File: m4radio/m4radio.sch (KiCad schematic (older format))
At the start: 71 parts, among them IC1 NCP4620, IC10 Si4460, IC2 MCP2562, IC3 STM32F405RxTx, IC4 MAX-M8Q, IC5 NC7SZ04, IC6 NCP380, IC7 CS2100-CP, IC8 SL18860DC, IC9 SN74LVC1G0832, J1 WEST TOP, J2 EAST TOP, P1 SWD_TC, P2 COAX, P3 COAX, Y1 TCXO

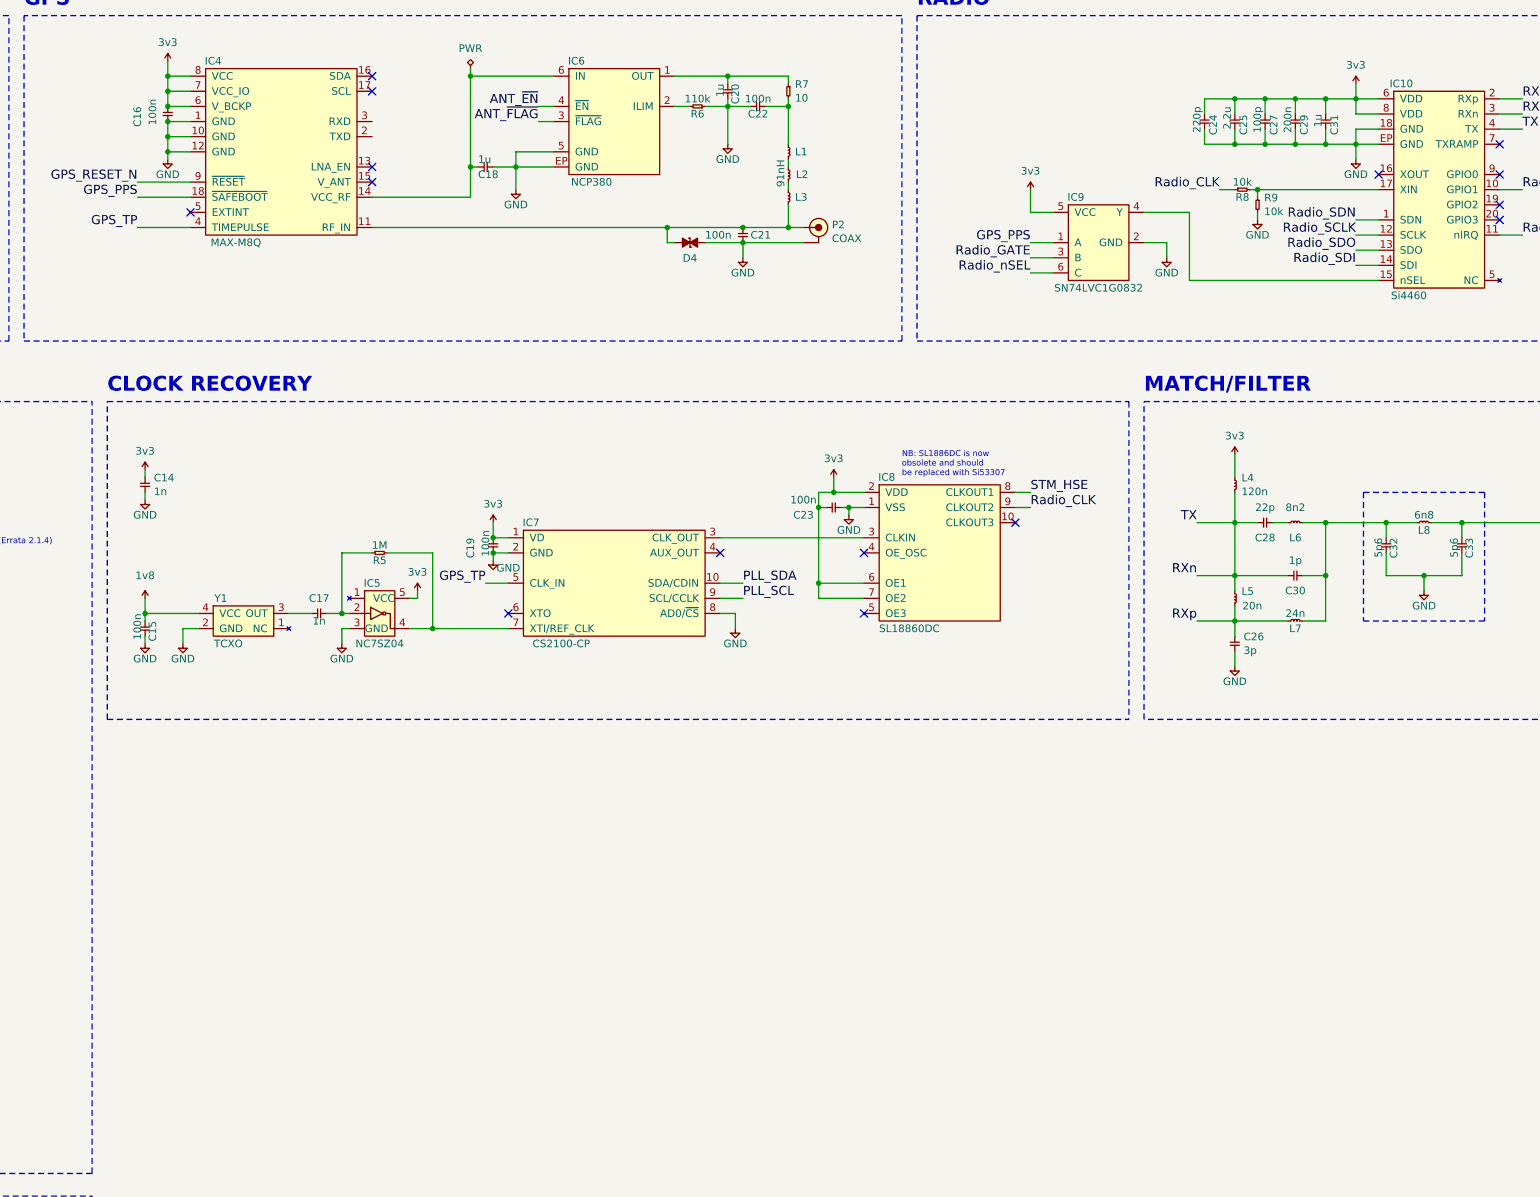
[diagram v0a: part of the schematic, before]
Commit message: Add power amp
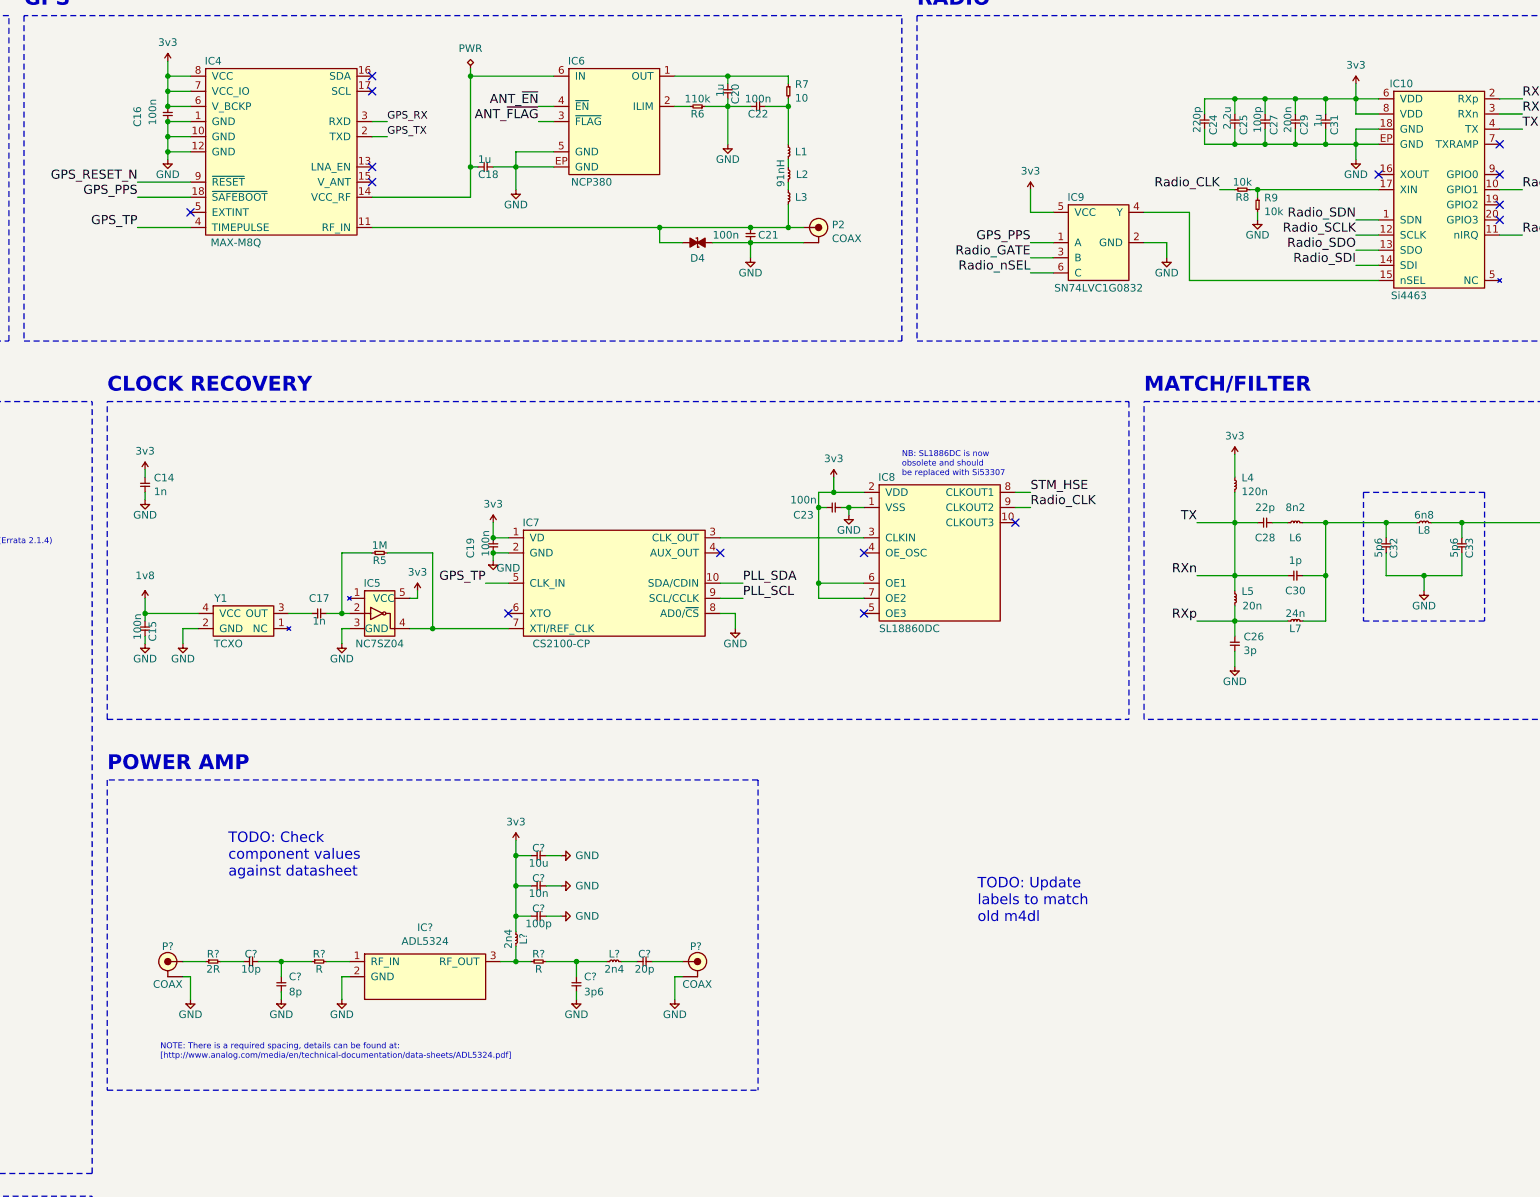
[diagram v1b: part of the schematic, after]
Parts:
- added C?: 8p, symbol cusf-kicad:C
- added C?: 10p, symbol cusf-kicad:C
- added C?: 3p6, symbol cusf-kicad:C
- added C?: 20p, symbol cusf-kicad:C
- added C?: 100p, symbol cusf-kicad:C
- added C?: 10n, symbol cusf-kicad:C
- added C?: 10u, symbol cusf-kicad:C
- added IC?: ADL5324, agg:SOT-89-3, symbol cusf-kicad:ADL5324
- added L? (x2): 2n4, symbol cusf-kicad:L
- added P? (x2): COAX, agg:SMA-EDGE, symbol cusf-kicad:COAX
- added R? (x2): R, symbol cusf-kicad:R
- added R?: 2R, symbol cusf-kicad:R
- IC10: value Si4460 -> Si4463
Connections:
- net 3v3: now also C?.1, C?.1, C?.1, L?.1
- net GND: now also C?.2, C?.2, C?.2, C?.2, C?.2, IC?.2 (GND), P?.2 (GND), P?.2 (GND)
- net GPS_RX: now also IC4.3 (RXD)
- net GPS_TX: now also IC4.2 (TXD)
- new net: IC?.1 (RF_IN), R?.2
- new net: IC?.3 (RF_OUT), L?.2, R?.1
- new net: C?.1, C?.2, R?.1
- new net: C?.1, R?.2
- new net: P?.1 (RF), R?.1
- new net: C?.1, L?.1, R?.2
- new net: C?.1, L?.2
- new net: C?.2, P?.1 (RF)
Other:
- note added: "NOTE: There is a required spacing, details can be found at:\n[http://www.analog.com/media/en/technical-documentation/data-sheets/ADL5324.pdf]"
- note added: "POWER AMP"
- note added: "TODO: Check\ncomponent values\nagainst datasheet"
- note added: "TODO: Update\nlabels to match\nold m4dl"
- moved on the sheet: C21, D4

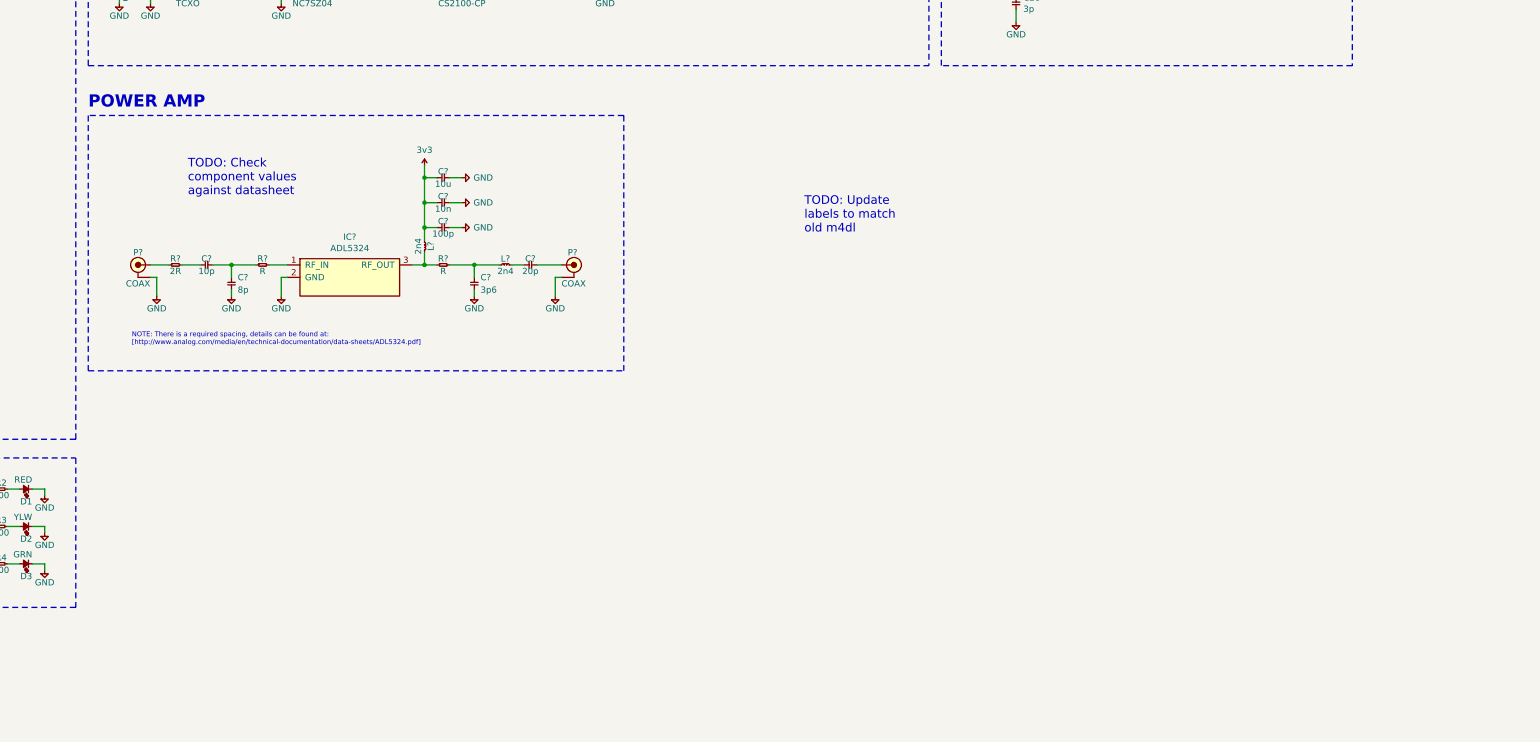
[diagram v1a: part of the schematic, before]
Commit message: Add GPS preamp
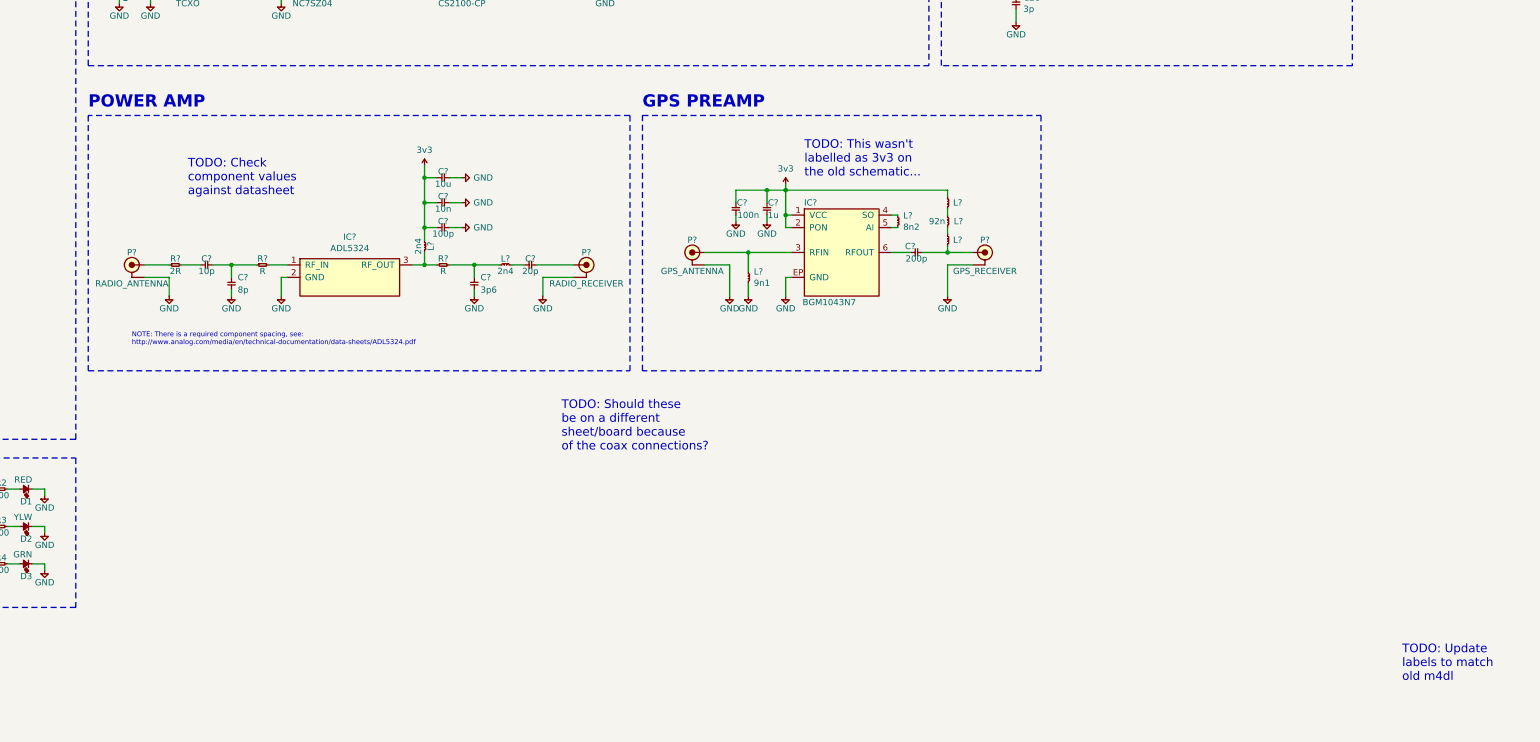
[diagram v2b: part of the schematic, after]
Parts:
- removed P?: COAX, agg:SMA-EDGE, symbol cusf-kicad:COAX
- added C?: 1u, symbol cusf-kicad:C
- added C?: 100n, symbol cusf-kicad:C
- added C?: 200p, symbol cusf-kicad:C
- added IC?: BGM1043N7, agg:DFN-6-EP-BGM, symbol cusf-kicad:BGM1043N7
- added L?: 9n1, symbol cusf-kicad:L
- added L?: 8n2, symbol cusf-kicad:L
- added L? (x3): 92n, symbol cusf-kicad:L
- added P?: GPS_ANTENNA, agg:SMA-EDGE, symbol cusf-kicad:COAX
- added P?: GPS_RECEIVER, agg:SMA-EDGE, symbol cusf-kicad:COAX
- added P?: RADIO_RECEIVER, agg:SMA-EDGE, symbol cusf-kicad:COAX
- P?: value COAX -> RADIO_ANTENNA
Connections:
- net 3v3: now also C?.1, C?.1, IC?.1 (VCC), IC?.2 (PON), L?.1
- net GND: now also C?.2, C?.2, IC?.EP (GND), L?.2, P?.2 (GND), P?.2 (GND), P?.2 (GND)
- net at C?.2: now also P?.1 (RF)
- new net: IC?.3 (RFIN), L?.1, P?.1 (RF)
- new net: IC?.4 (SO), L?.1
- new net: IC?.5 (AI), L?.2
- new net: C?.1, IC?.6 (RFOUT)
- new net: C?.2, L?.2, P?.1 (RF)
- new net: L?.1, L?.2 (x2)
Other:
- note added: "GPS PREAMP"
- note added: "NOTE: There is a required component spacing, see:\nhttp://www.analog.com/media/en/technical-documentation/data-sheets/ADL5324.pdf"
- note added: "TODO: Should these\nbe on a different\nsheet/board because\nof the coax connections?"
- note added: "TODO: This wasn't\nlabelled as 3v3 on\nthe old schematic..."
- note removed: "NOTE: There is a required spacing, details can be found at:\n[http://www.analog.com/media/en/technical-documentation/data-sheets/ADL5324.pdf]"
- moved on the sheet: P?
